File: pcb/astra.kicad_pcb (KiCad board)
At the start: 2 copper layers, 82 parts, among them J1 Conn_01x02_Pin, J2 Conn_01x24_MountingPin, J3 Conn_02x10_Odd_Even, M1 Motor_DC, M2 Motor_DC, M3 Motor_DC, M4 Motor_DC, Q1 AO3400A, Q2 AO3400A, Q3 AO3400A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

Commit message: [pcb] more routing
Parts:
- C2, C22, C23, C25, C26, C27, SW3, U4, U6: moved to B.Cu
- R3: moved to F.Cu
- moved C2 20.9 mm to (145.2, 57.6), turned to 0 degrees
- moved C25 12.2 mm to (148.2, 35.4)
- moved C23 11.9 mm to (133.8, 43.2)
- moved U6 7.60 mm to (147.7, 38.1)
- moved C26 7.60 mm to (144.3, 38.1), turned to -90 degrees
- moved C22 7.08 mm to (136.3, 46.1), turned to 180 degrees
- moved C27 6.80 mm to (130.7, 41.7)
- moved U4 5.01 mm to (137.3, 43.3), turned to 180 degrees
- moved FB2 4.17 mm to (128.8, 43.8)
- moved J2 3.65 mm to (141.5, 38.1)
- moved C31 3.32 mm to (136.4, 46.3), turned to 90 degrees
- moved C24 3.25 mm to (135.3, 37.9)
- moved C28 3.25 mm to (142.1, 37.9)
- moved R13 3.25 mm to (133.2, 38.0)
- moved R15 3.25 mm to (139.8, 37.9)
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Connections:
- U3 pad 63: DCMI_D0 -> unconnected-(U3-PC6-Pad63)
- U3 pad 65: DCMI_D2 -> unconnected-(U3-PC8-Pad65)
- U3 pad 66: DCMI_D3 -> unconnected-(U3-PC9-Pad66)
- U3 pad 68: unconnected-(U3-PA9-Pad68) -> DCMI_D0
- U3 pad 97: unconnected-(U3-PE0-Pad97) -> DCMI_D2
- U3 pad 98: unconnected-(U3-PE1-Pad98) -> DCMI_D3
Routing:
- net +3.3V: track 108.8 -> 140.5 mm
- net DCMI_HSYNC: track 0.00 -> 24.8 mm, vias 0 -> 2
- net DCMI_PCLK: track 0.00 -> 23.1 mm, vias 0 -> 2
- net FLASH_CS: track 0.00 -> 21.1 mm, vias 0 -> 2
- net DCMI_XCLK: track 0.00 -> 19.2 mm, vias 0 -> 2
- net DCMI_D6: track 0.00 -> 18.9 mm, vias 0 -> 3
- net DCMI_D3: track 0.00 -> 18.7 mm, vias 0 -> 2
- net DCMI_D7: track 0.00 -> 18.3 mm, vias 0 -> 2
- net FLASH_IO_3: track 0.00 -> 17.4 mm
- net DCMI_D2: track 0.00 -> 16.0 mm, vias 0 -> 2
- net DCMI_D1: track 0.00 -> 15.5 mm
- net QSPI_CLK: track 0.00 -> 15.2 mm
- net DCMI_D0: track 0.00 -> 12.5 mm
- net +BATT: track 0.00 -> 12.4 mm
- net DCMI_SDA: track 2.95 -> 15.2 mm
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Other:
- board outline added: 43 x 39.8 mm

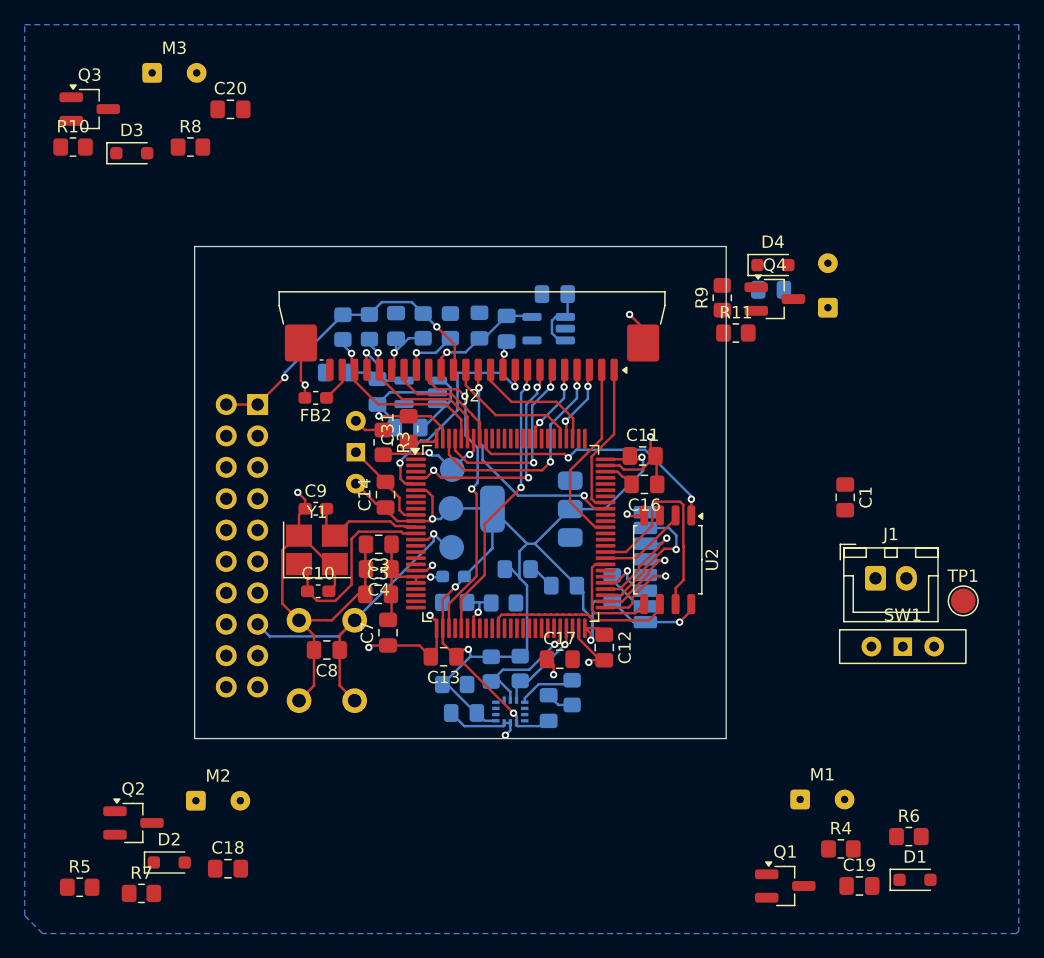
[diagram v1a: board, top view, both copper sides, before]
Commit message: [pcb] 4 layer routing
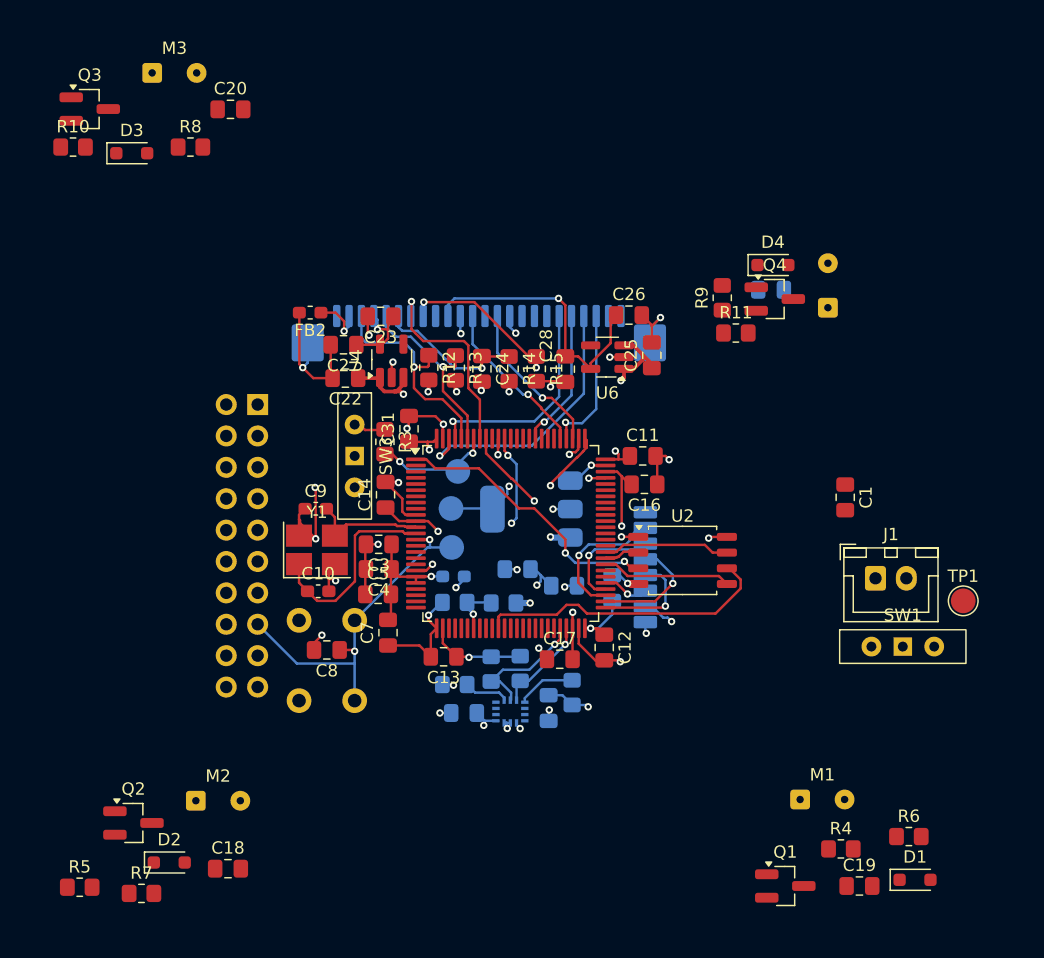
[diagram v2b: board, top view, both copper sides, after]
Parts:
- C22, C23, C24, C25, C26, C27, C28, R12, R13, R14, R15, SW3, U4, U6: moved to F.Cu
- J2: moved to B.Cu
- moved C26 9.96 mm to (154.2, 37.0), turned to 0 degrees
- moved C25 9.28 mm to (156.1, 40.3), turned to 90 degrees
- moved C28 7.79 mm to (149.1, 41.4), turned to -90 degrees
- moved C24 7.77 mm to (142.3, 41.4), turned to -90 degrees
- moved R14 7.77 mm to (144.5, 41.4), turned to -90 degrees
- moved R15 7.77 mm to (146.7, 41.4), turned to -90 degrees
- moved R13 7.70 mm to (140.2, 41.3), turned to -90 degrees
- moved R12 7.68 mm to (138.0, 41.3), turned to -90 degrees
- moved FB2 6.91 mm to (128.4, 36.9)
- moved C22 6.43 mm to (131.2, 42.1)
- moved C23 6.11 mm to (134.1, 37.1), turned to 180 degrees
- moved U6 5.28 mm to (152.4, 40.5)
- moved U4 3.47 mm to (135.0, 40.8), turned to 90 degrees
- moved J2 2.46 mm to (142.1, 40.5)
- moved C27 2.29 mm to (131.1, 39.5)
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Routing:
- net +3.3V: track 140.5 -> 46.3 mm, vias 9 -> 20
- net TDO: track 0.00 -> 32.9 mm, vias 0 -> 2
- net TCLK: track 0.00 -> 30.3 mm, vias 0 -> 1
- net TDI: track 0.00 -> 30.1 mm, vias 0 -> 1
- net TMS: track 0.00 -> 29.7 mm, vias 0 -> 1
- net +BATT: track 12.4 -> 40.5 mm, vias 0 -> 4
- net TRST: track 0.00 -> 27.9 mm, vias 0 -> 1
- net DCMI_HSYNC: track 24.8 -> 0.00 mm, vias 2 -> 0
- net DCMI_PCLK: track 23.1 -> 0.00 mm, vias 2 -> 0
- net FLASH_IO_2: track 0.00 -> 22.4 mm, vias 0 -> 2
- net DCMI_XCLK: track 19.2 -> 0.00 mm, vias 2 -> 0
- net GND: track 112.0 -> 93.0 mm, vias 13 -> 28
- net DCMI_D6: track 18.9 -> 0.00 mm, vias 3 -> 0
- net DCMI_D7: track 18.3 -> 0.00 mm, vias 2 -> 0
- net Net-(C16-Pad2): track 2.53 -> 19.0 mm, vias 0 -> 2
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- added copper zone on In2.Cu, net +3.3V
- added copper zone on In1.Cu, net GND
- removed copper zone on B.Cu, net GND
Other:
- board outline removed
- copper layers 2 -> 4

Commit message: [pcb] continue routing - motors, camera, battery
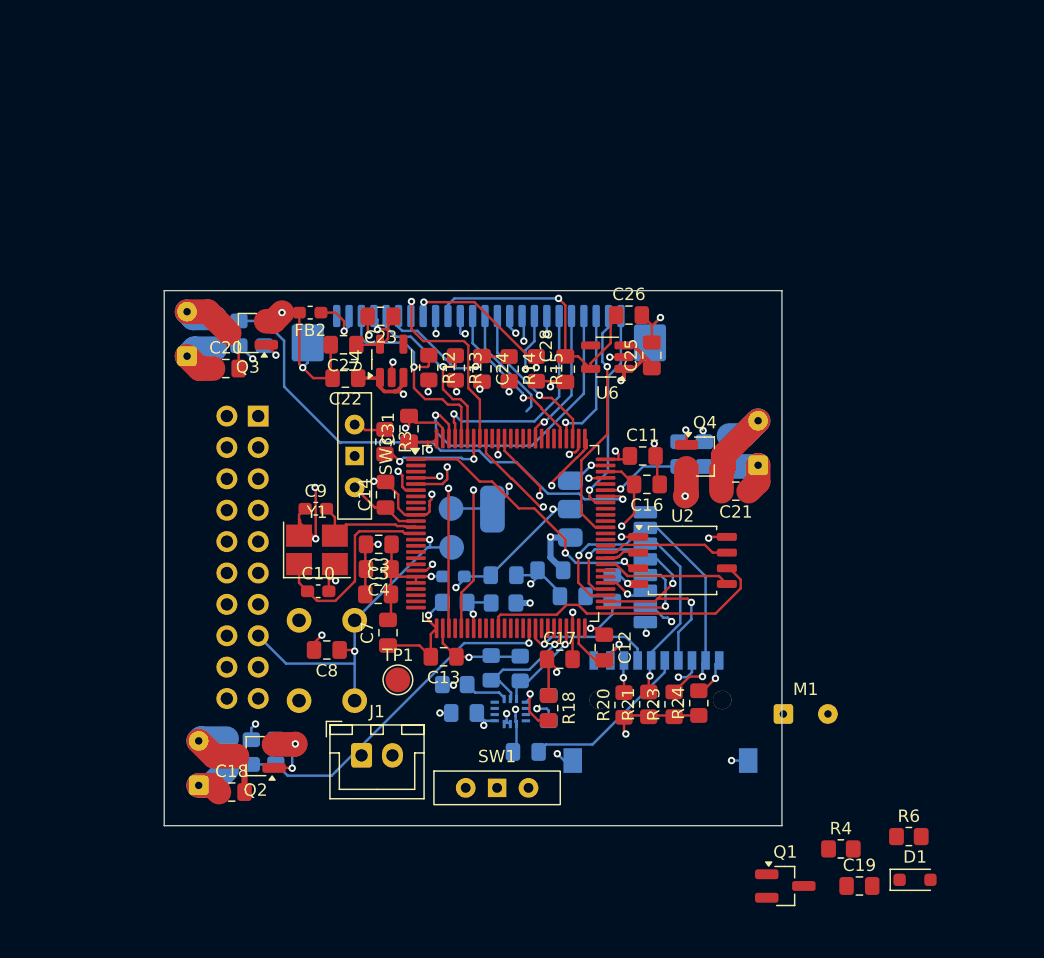
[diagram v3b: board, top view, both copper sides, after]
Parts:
- removed TP4: TP_BOOT, TestPoint:TestPoint_Pad_D2.0mm
- added C32: 100nF, Capacitor_SMD:C_0805_2012Metric_Pad1.18x1.45mm_HandSolder, B.Cu at (145.8, 72.4)
- added R20: 10k, Resistor_SMD:R_0805_2012Metric_Pad1.20x1.40mm_HandSolder, F.Cu at (153.8, 68.6)
- added R21: 10k, Resistor_SMD:R_0805_2012Metric_Pad1.20x1.40mm_HandSolder, F.Cu at (155.8, 68.5)
- added R23: 10k, Resistor_SMD:R_0805_2012Metric_Pad1.20x1.40mm_HandSolder, F.Cu at (157.8, 68.5)
- added R24: 10k, Resistor_SMD:R_0805_2012Metric_Pad1.20x1.40mm_HandSolder, F.Cu at (159.8, 68.5)
- added U8: HYCW110-TF10-180B, lcsc:SIM-SMD_HYCW110-TF10-180B, B.Cu at (156.8, 69.0)
- C1, D2, D3, D4, M2, M3, R10, R11, R5, R7, R8, R9: moved to B.Cu
- C21, R18: moved to F.Cu
- U7: footprint lcsc:LGA-14_L3.0-W2.5-P0.50-BR -> Package_LGA:Bosch_LGA-14_3x2.5mm_P0.5mm
- moved TP1 46.2 mm to (135.5, 66.6)
- moved J1 44.0 mm to (132.6, 72.7)
- moved SW1 34.8 mm to (143.5, 75.3)
- moved C1 24.6 mm to (147.8, 57.7), turned to 0 degrees
- moved M3 23.1 mm to (118.4, 40.4), turned to 90 degrees
- moved Q3 22.2 mm to (123.3, 38.5), turned to 180 degrees
- moved C20 21.0 mm to (121.6, 41.4)
- moved R10 20.2 mm to (122.6, 38.5), turned to -90 degrees
- moved R5 19.3 mm to (125.6, 72.4), turned to 90 degrees
- moved C21 16.5 mm to (162.8, 51.3), turned to 180 degrees
- moved R8 16.2 mm to (124.7, 38.5), turned to -90 degrees
- moved D3 16.1 mm to (120.7, 38.5), turned to 90 degrees
- moved D4 15.5 mm to (162.3, 48.0), turned to 90 degrees
- moved R7 14.5 mm to (123.6, 72.4), turned to 90 degrees
- moved M4 13.9 mm to (164.7, 49.2)
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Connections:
- U3 pad 42: unconnected-(U3-PE12-Pad42) -> CS_SD
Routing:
- net MOTOR3: track 0.00 -> 40.7 mm, vias 0 -> 1
- net +3.3V: track 46.3 -> 77.8 mm, vias 20 -> 19
- net +BATT: track 40.5 -> 70.0 mm
- net MOTOR2: track 0.00 -> 28.5 mm, vias 0 -> 1
- net DCMI_PCLK: track 0.00 -> 27.7 mm, vias 0 -> 2
- net DCMI_HSYNC: track 0.00 -> 27.3 mm, vias 0 -> 2
- net GND: track 93.0 -> 116.0 mm, vias 28 -> 36
- net DCMI_D1: track 0.00 -> 19.6 mm, vias 0 -> 1
- net DCMI_D6: track 0.00 -> 18.9 mm, vias 0 -> 2
- net DCMI_D7: track 0.00 -> 18.5 mm, vias 0 -> 2
- net SPI2_MISO: track 11.4 -> 28.9 mm, vias 1 -> 2
- net DCMI_D0: track 0.00 -> 17.2 mm, vias 0 -> 1
- net SPI2_MOSI: track 8.78 -> 23.6 mm, vias 1 -> 2
- net Net-(U8-VDD): track 0.00 -> 13.8 mm
- net CS_SD: track 0.00 -> 10.9 mm, vias 0 -> 1
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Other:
- board outline added: 50 x 43.3 mm

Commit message: [pcb] changed switches to optimize pcb layout
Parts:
- removed SW3: SW_SPDT, Button_Switch_THT:SW_Slide-03_Wuerth-WS-SLTV_10x2.5x6.4_P2.54mm
- added J4: Conn_02x05_Odd_Even, Connector_PinHeader_2.54mm:PinHeader_2x05_P2.54mm_Vertical, F.Cu at (119.0, 55.5)
- added JP1: SolderJumper_3_Open, Jumper:SolderJumper-3_P1.3mm_Open_RoundedPad1.0x1.5mm, B.Cu at (134.5, 48.2)
- added X1: OT322524MJBA4SL, Crystal:Crystal_SMD_3225-4Pin_3.2x2.5mm_HandSoldering, F.Cu at (162.6, 38.6)
- J3: value Conn_02x10_Odd_Even -> Conn_02x04_Odd_Even; footprint Connector_PinHeader_2.54mm:PinHeader_2x10_P2.54mm_Vertical -> Connector_PinHeader_2.54mm:PinHeader_2x04_P2.54mm_Vertical; moved to F.Cu
- SW1: value SW_SPDT -> SS-3235S-L1; footprint Button_Switch_THT:SW_Slide-03_Wuerth-WS-SLTV_10x2.5x6.4_P2.54mm -> lcsc:SW-SMD_SS-3235S-LX; moved to B.Cu
- moved SW1 25.9 mm to (127.5, 55.0)
- moved J3 5.29 mm to (120.5, 49.0), turned to 90 degrees
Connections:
- J1 pad 1: Net-(J1-Pin_1) -> +BATT
- J3 pad 1: +3.3V -> TRST
- J3 pad 3: TRST -> TDI
- J3 pad 5: TDI -> TMS
- J3 pad 6: GND -> TDO
- J3 pad 7: TMS -> TCLK
- J3 pad 8: GND -> RST
- SW1 pad 1: unconnected-(SW1-A-Pad1) -> SPI2_MISO
- SW1 pad 2: Net-(J1-Pin_1) -> MISO_SCL
- SW1 pad 3: +BATT -> IMU_SCL
- U3 pad 18: unconnected-(U3-PC3_C-Pad18) -> DDG_MAGIC_1
- U3 pad 22: unconnected-(U3-PA0-Pad22) -> DDG_MAGIC_2
- U3 pad 23: unconnected-(U3-PA1-Pad23) -> DDG_MAGIC_3
- U3 pad 24: unconnected-(U3-PA2-Pad24) -> DDG_MAGIC_4
- U3 pad 25: unconnected-(U3-PA3-Pad25) -> DDG_MAGIC_5
- U3 pad 61: DCMI_PWDN -> unconnected-(U3-PD14-Pad61)
- U3 pad 62: DCMI_RST -> unconnected-(U3-PD15-Pad62)
- U3 pad 67: DCMI_XCLK -> unconnected-(U3-PA8-Pad67)
- U3 pad 87: unconnected-(U3-PD6-Pad87) -> DCMI_PWDN
- U3 pad 88: unconnected-(U3-PD7-Pad88) -> DCMI_RST

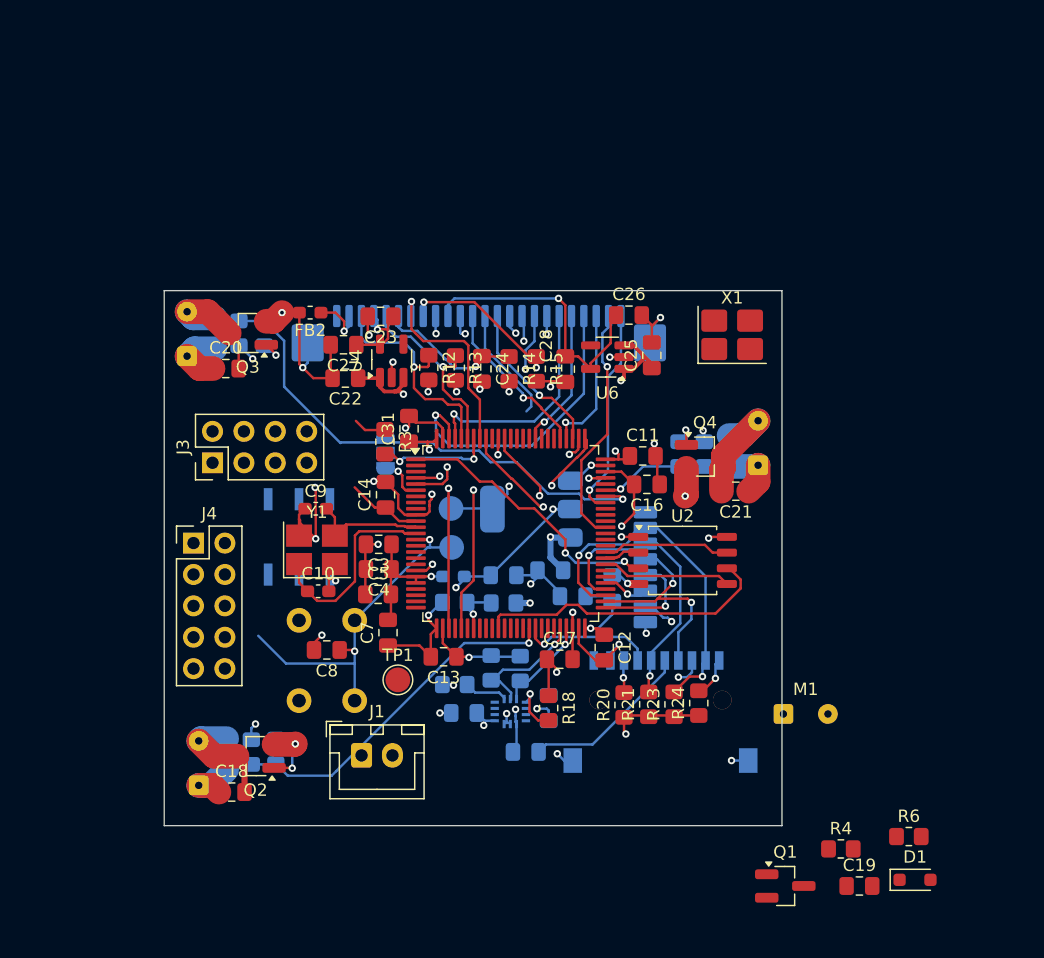
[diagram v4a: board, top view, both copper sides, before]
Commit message: [pcb] finish routing
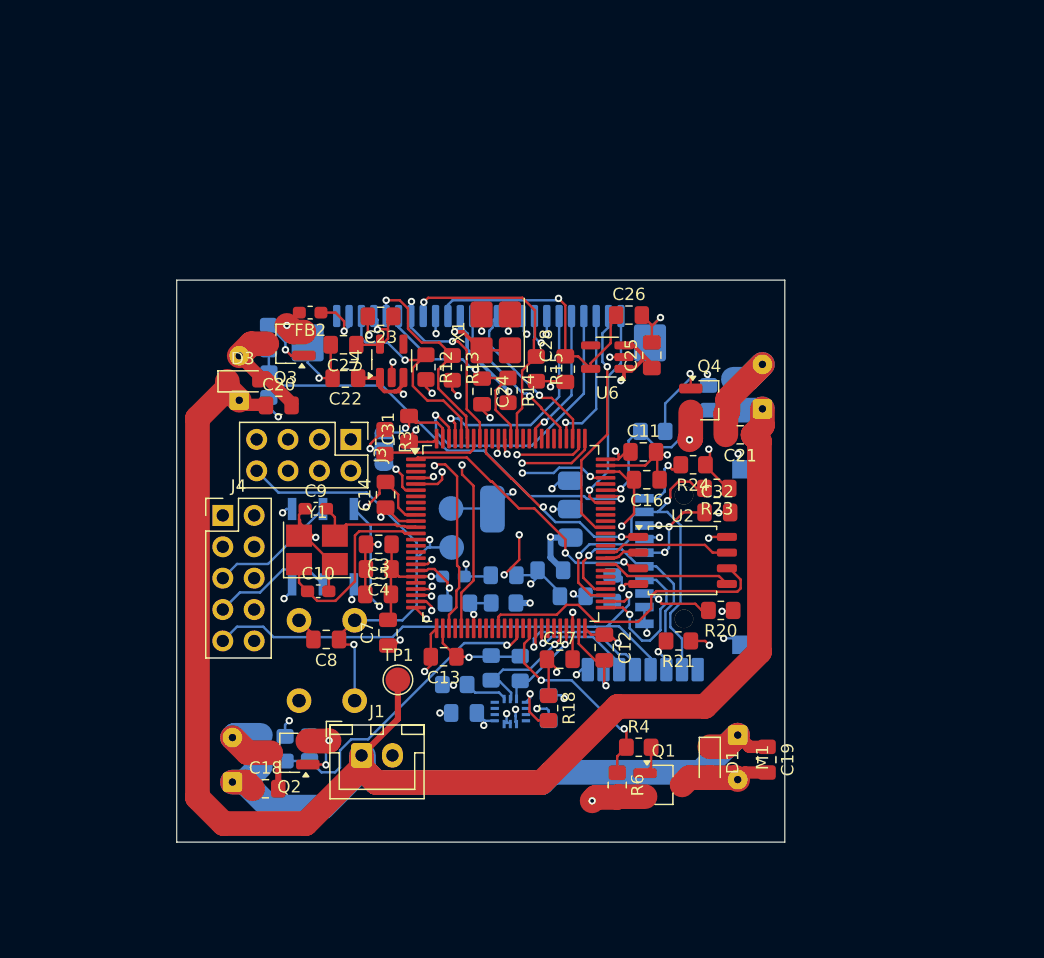
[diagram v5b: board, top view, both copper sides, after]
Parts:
- C32, D3: moved to F.Cu
- moved C32 24.8 mm to (161.3, 53.0)
- moved R6 24.0 mm to (153.2, 75.1), turned to -90 degrees
- moved R24 19.3 mm to (159.4, 49.2), turned to 180 degrees
- moved D1 19.1 mm to (160.7, 73.2), turned to -90 degrees
- moved X1 19.1 mm to (143.4, 38.5), turned to 90 degrees
- moved R4 18.3 mm to (155.0, 72.0)
- moved U5 18.1 mm to (154.8, 73.8), turned to -90 degrees
- moved R23 17.8 mm to (161.3, 51.1), turned to 180 degrees
- moved Q1 12.8 mm to (157.0, 75.1)
- moved U8 12.7 mm to (159.5, 56.6), turned to -90 degrees
- moved C19 12.7 mm to (165.4, 73.0), turned to -90 degrees
- moved J3 11.3 mm to (131.7, 47.1), turned to -90 degrees
- moved R20 10.9 mm to (161.6, 61.0), turned to 180 degrees
- moved R21 5.66 mm to (158.2, 63.4), turned to 180 degrees
- moved M3 5.53 mm to (122.7, 43.9)
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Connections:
- C32 pad 2: Net-(U8-VDD) -> GND
- J3 pad 2: +3.3V -> TDO
- J3 pad 4: GND -> TCLK
- J3 pad 5: TMS -> GND
- J3 pad 6: TDO -> TMS
- J3 pad 7: TCLK -> +3.3V
- J4 pad 1: DDG_MAGIC_1 -> +3.3V
- J4 pad 10: SPI2_CLK -> DDG_MAGIC_5
- J4 pad 2: +3.3V -> DDG_MAGIC_1
- J4 pad 3: DDG_MAGIC_2 -> GND
- J4 pad 4: GND -> DDG_MAGIC_2
- J4 pad 5: DDG_MAGIC_3 -> MOSI_SDA
- J4 pad 6: MISO_SCL -> DDG_MAGIC_3
- J4 pad 7: DDG_MAGIC_4 -> MISO_SCL
- J4 pad 8: MOSI_SDA -> DDG_MAGIC_4
- J4 pad 9: DDG_MAGIC_5 -> SPI2_CLK
- U3 pad 39: MOTOR1 -> MOTOR2
- U3 pad 41: MOTOR2 -> MOTOR1
- U3 pad 42: CS_SD -> NRF_CS
- U3 pad 43: unconnected-(U3-PE13-Pad43) -> NRF_CE
- U3 pad 51: NRF_CS -> CS_SD
- U3 pad 55: NRF_CE -> unconnected-(U3-PD8-Pad55)
- U8 pad 4: Net-(U8-VDD) -> +3.3V
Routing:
- net +BATT: track 70.0 -> 253.4 mm
- net SPI2_MISO: track 28.9 -> 65.6 mm, vias 2 -> 3
- net SPI2_CLK: track 17.5 -> 51.4 mm
- net SPI2_MOSI: track 23.6 -> 50.8 mm, vias 2 -> 3
- net IMU_SDA: track 7.89 -> 34.0 mm, vias 1 -> 2
- net DDG_MAGIC_5: track 0.00 -> 19.9 mm, vias 0 -> 1
- net DDG_MAGIC_4: track 0.00 -> 19.7 mm, vias 0 -> 1
- net IMU_SCL: track 10.4 -> 30.1 mm, vias 1 -> 2
- net DDG_MAGIC_1: track 0.00 -> 18.5 mm, vias 0 -> 1
- net TDO: track 34.9 -> 16.5 mm
- net DDG_MAGIC_2: track 0.00 -> 17.7 mm, vias 0 -> 1
- net MOTOR1: track 0.00 -> 17.3 mm, vias 0 -> 2
- net DDG_MAGIC_3: track 0.00 -> 16.7 mm, vias 0 -> 1
- net Net-(U8-VDD): track 13.8 -> 0.00 mm
- net TRST: track 27.3 -> 15.7 mm
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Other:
- board size 50 x 43.3 mm -> 49.2 x 45.5 mm
